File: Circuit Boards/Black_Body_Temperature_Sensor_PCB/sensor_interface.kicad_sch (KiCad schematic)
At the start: 5 parts, among them J1 Conn_01x04_Pin, Q8 TMUX1112PWR, Q9 TMUX1112PWR

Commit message: power simulation
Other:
- moved on the sheet: J1, Q8, Q9, R16, R17

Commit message: Schematic ready for review
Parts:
- added Q10: TMUX1112PWR, Package_SO:TSSOP-16_4.4x5mm_P0.65mm, symbol -fet:TMUX1112PWR
- added R36: 5, symbol Device:R
- added R37: 500, symbol Device:R
- added R38: 35k, symbol Device:R
- R16, R17: now not fitted
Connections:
- net +3V3: now also Q10.13 (VDD)
- net GNDPWR: now also Q10.5 (GND)
- net i+: now also Q10.2 (D1), R36.1, R37.1, R38.1; no longer Q8.15 (D2), Q8.2 (D1)
- new net: Q10.15 (D2), R36.2
- new net: Q10.7 (D4), R38.2
- new net: Q10.10 (D3), R37.2
- new net: Q10.12 (NC), Q10.4 (NC)
- new net i_sense.I+: Q10.11 (S3), Q10.14 (S2), Q10.3 (S1), Q10.6 (S4), Q8.15 (D2), Q8.2 (D1)
- new net i_sense_sel1: Q10.1 (SEL1)
- new net i_sense_sel2: Q10.16 (SEL2)
- new net i_sense_sel3: Q10.9 (SEL3)
- new net i_sense_sel4: Q10.8 (SEL4)
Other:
- moved on the sheet: Q8, Q9

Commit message: Temp sensor schematic done
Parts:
- removed J1: Conn_01x04_Pin, symbol Connector:Conn_01x04_Pin
- added J401, J402: Screw_Terminal_01x02, TerminalBlock_MetzConnect:TerminalBlock_MetzConnect_Type011_RT05502HBLC_1x02_P5.00mm_Horizontal, symbol Connector:Screw_Terminal_01x02
- R401: renamed from R36; footprint (none) -> Resistor_SMD:R_0603_1608Metric
- R402: renamed from R37; footprint (none) -> Resistor_SMD:R_0603_1608Metric
- R403: renamed from R38; footprint (none) -> Resistor_SMD:R_0603_1608Metric
- R404: renamed from R16; footprint (none) -> Resistor_SMD:R_0603_1608Metric
- R405: renamed from R17; footprint (none) -> Resistor_SMD:R_0603_1608Metric
- renumbered Q10 to Q401, Q8 to Q402, Q9 to Q403
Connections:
- net i+: now also J402.1 (Pin_1)
- net i-: now also J402.2 (Pin_2)
- net v_sense.V+: now also J401.1 (Pin_1)
- net v_sense.V-: now also J401.2 (Pin_2)
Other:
- note added: "Sensor Interface (PAGE 4)"
- moved on the sheet: Q401, Q402, Q403, R401, R402, R403, R404, R405

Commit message: temp pcb analog layout done
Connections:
- net GND: now also Q402.3 (S1); no longer Q402.14 (S2)
- net i-: now also Q402.15 (D2), Q402.2 (D1); no longer Q402.10 (D3), Q402.7 (D4)
- net i_sense.I+: now also Q402.10 (D3), Q402.7 (D4); no longer Q402.15 (D2), Q402.2 (D1)
- net at R404.1: now also Q403.3 (S1); no longer Q403.14 (S2)
- net I_Source: now reaches Q402.11 (S3), Q403.11 (S3)
- net I_Source: now also Q402.14 (S2), Q403.14 (S2)

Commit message: Digital section done
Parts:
- J401, J402: footprint TerminalBlock_MetzConnect:TerminalBlock_MetzConnect_Type011_RT05502HBLC_1x02_P5.00mm_Horizontal -> -connector:CUI_TB002-500-02BE
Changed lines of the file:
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@@
 			)
 		)
-		(property "Footprint" "TerminalBlock_MetzConnect:TerminalBlock_MetzConnect_Type011_RT05502HBLC_1x02_P5.00mm_Horizontal"
+		(property "Footprint" "-connector:CUI_TB002-500-02BE"
 			(at 50.8 101.6 0)
 			(hide yes)
@@
 	)
 	(symbol
+		(lib_id "Connector:Screw_Terminal_01x02")
+		(at 50.8 106.68 0)
+		(mirror y)
+		(unit 1)
+		(body_style 1)
+		(exclude_from_sim no)
+		(in_bom yes)
+		(on_board yes)
+		(in_pos_files yes)
+		(dnp no)
+		(property "Reference" "J402"
+			(at 48.26 106.6799 0)
+			(show_name no)
+			(do_not_autoplace no)
+			(effects
+				(font
+					(size 1.27 1.27)
+				)
+				(justify left)
+			)
+		)
+		(property "Value" "Screw_Terminal_01x02"
+			(at 48.26 109.2199 0)
+			(show_name no)
+			(do_not_autoplace no)
+			(effects
+				(font
+					(size 1.27 1.27)
+				)
+				(justify left)
+			)
+		)
+		(property "Footprint" "-connector:CUI_TB002-500-02BE"
+			(at 50.8 106.68 0)
+			(hide yes)
+			(show_name no)
+			(do_not_autoplace no)
+			(effects
+				(font
+					(size 1.27 1.27)
+				)
+			)
+		)
+		(property "Datasheet" ""
+			(at 50.8 106.68 0)
+			(hide yes)
+			(show_name no)
+			(do_not_autoplace no)
+			(effects
+				(font
+					(size 1.27 1.27)
+				)
+			)
+		)
+		(property "Description" "Generic screw terminal, single row, 01x02, script generated (kicad-library-utils/schlib/autogen/connector/)"
+			(at 50.8 106.68 0)
+			(hide yes)
+			(show_name no)
+			(do_not_autoplace no)
+			(effects
+				(font
+					(size 1.27 1.27)
+				)
+			)
+		)
+		(pin "1"
+		)
+		(pin "2"
+		)
+		(instances
+			(project "Black_Body_Temperature_Sensor_PCB"
+				(path "/e46fba8d-0294-4f4f-927d-8614bb9d51d3/4094c958-ded6-41d9-bb08-a88dca4a947b"
+					(reference "J402")
+					(unit 1)
+				)
+			)
+		)
+	)
+	(symbol
 		(lib_id "Device:R")
 		(at 104.14 82.55 90)
@@
 					(unit 1)
 				)
-			)
-		)
-	)
-	(symbol
-		(lib_id "Connector:Screw_Terminal_01x02")
-		(at 50.8 106.68 0)
-		(mirror y)
-		(unit 1)
-		(body_style 1)
-		(exclude_from_sim no)
-		(in_bom yes)
-		(on_board yes)
-		(in_pos_files yes)
-		(dnp no)
-		(property "Reference" "J402"
-			(at 48.26 106.6799 0)
-			(show_name no)
-			(do_not_autoplace no)
-			(effects
-				(font
-					(size 1.27 1.27)
-				)
-				(justify left)
-			)
-		)
-		(property "Value" "Screw_Terminal_01x02"
-			(at 48.26 109.2199 0)
-			(show_name no)
-			(do_not_autoplace no)
-			(effects
-				(font
-					(size 1.27 1.27)
-				)
-				(justify left)
-			)
-		)
-		(property "Footprint" "TerminalBlock_MetzConnect:TerminalBlock_MetzConnect_Type011_RT05502HBLC_1x02_P5.00mm_Horizontal"
-			(at 50.8 106.68 0)
-			(hide yes)
-			(show_name no)
-			(do_not_autoplace no)
-			(effects
-				(font
-					(size 1.27 1.27)
-				)
-			)
-		)
-		(property "Datasheet" ""
-			(at 50.8 106.68 0)
-			(hide yes)
-			(show_name no)
-			(do_not_autoplace no)
-			(effects
-				(font
-					(size 1.27 1.27)
-				)
-			)
-		)
-		(property "Description" "Generic screw terminal, single row, 01x02, script generated (kicad-library-utils/schlib/autogen/connector/)"
-			(at 50.8 106.68 0)
-			(hide yes)
-			(show_name no)
-			(do_not_autoplace no)
-			(effects
-				(font
-					(size 1.27 1.27)
-				)
-			)
-		)
-		(pin "1"
-		)
-		(pin "2"
-		)
-		(instances
-			(project "Black_Body_Temperature_Sensor_PCB"
-				(path "/e46fba8d-0294-4f4f-927d-8614bb9d51d3/4094c958-ded6-41d9-bb08-a88dca4a947b"
-					(reference "J402")
-					(unit 1)
-				)

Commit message: Complete except for recommended changes
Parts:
- added C401, C402, C403, C404, C405, C406, C407, C408, C409, C410, C411, C412, C413, C414, C415, C416, C417, C418, C419, C420, C421, C422, C423, C424: 2u2, Capacitor_SMD:C_0402_1005Metric, symbol Device:C
- added R401, R402, R403, R404, R408, R409, R410, R411, R414, R415, R416, R417: 5.1k, Resistor_SMD:R_0402_1005Metric, symbol Device:R
- added TP401, TP402, TP403: TestPoint, TestPoint:TestPoint_Pad_2.0x2.0mm, symbol Connector:TestPoint
- renumbered R401 to R405, R402 to R406, R403 to R407, R404 to R412, R405 to R413
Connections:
- net GNDPWR: now also C401.2, C402.2, C403.2, C404.2, C405.2, C406.2, C407.2, C408.2, C409.2, C410.2, C411.2, C412.2, C413.2, C414.2, C415.2, C416.2, C417.2, C418.2, C419.2, C420.2, C421.2, C422.2, C423.2, C424.2
- net I_Source: now also TP401.1
- net hbridge_sel1: now also C413.1, R408.2; no longer Q402.1 (SEL1)
- net hbridge_sel2: now also C414.1, R409.2; no longer Q402.16 (SEL2)
- net hbridge_sel3: now also C415.1, R410.2; no longer Q402.9 (SEL3)
- net hbridge_sel4: now also C416.1, R411.2; no longer Q402.8 (SEL4)
- net i_sense_sel1: now also C405.1, R401.2; no longer Q401.1 (SEL1)
- net i_sense_sel2: now also C406.1, R402.2; no longer Q401.16 (SEL2)
- net i_sense_sel3: now also C407.1, R403.2; no longer Q401.9 (SEL3)
- net i_sense_sel4: now also C408.1, R404.2; no longer Q401.8 (SEL4)
- net i_source_sel1: now also C421.1, R414.2; no longer Q403.1 (SEL1)
- net i_source_sel2: now also C422.1, R415.2; no longer Q403.16 (SEL2)
- net i_source_sel3: now also C423.1, R416.2; no longer Q403.9 (SEL3)
- net i_source_sel4: now also C424.1, R417.2; no longer Q403.8 (SEL4)
- net nA_I_Source: now also TP403.1
- net uA_I_Source: now also TP402.1
- new net selh1: C409.1, Q402.1 (SEL1), R408.1
- new net selh2: C410.1, Q402.16 (SEL2), R409.1
- new net selh3: C411.1, Q402.9 (SEL3), R410.1
- new net selh4: C412.1, Q402.8 (SEL4), R411.1
- new net seli1: C401.1, Q401.1 (SEL1), R401.1
- new net seli2: C402.1, Q401.16 (SEL2), R402.1
- new net seli3: C403.1, Q401.9 (SEL3), R403.1
- new net seli4: C404.1, Q401.8 (SEL4), R404.1
- new net sels1: C417.1, Q403.1 (SEL1), R414.1
- new net sels2: C418.1, Q403.16 (SEL2), R415.1
- new net sels3: C419.1, Q403.9 (SEL3), R416.1
- new net sels4: C420.1, Q403.8 (SEL4), R417.1

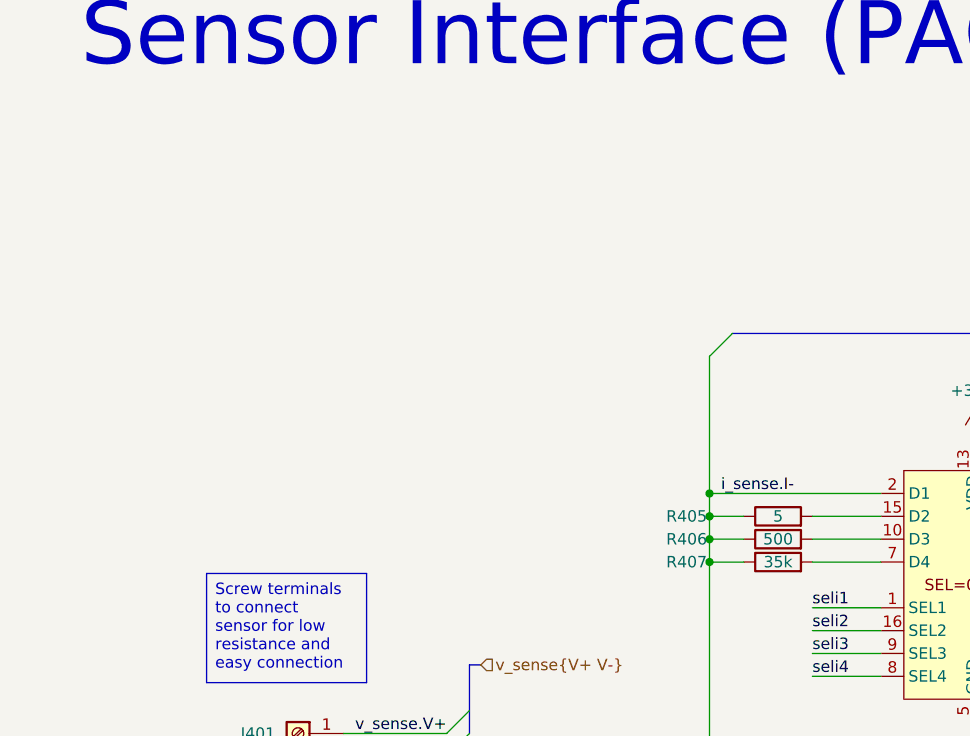
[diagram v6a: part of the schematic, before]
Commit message: Temp probe bom done
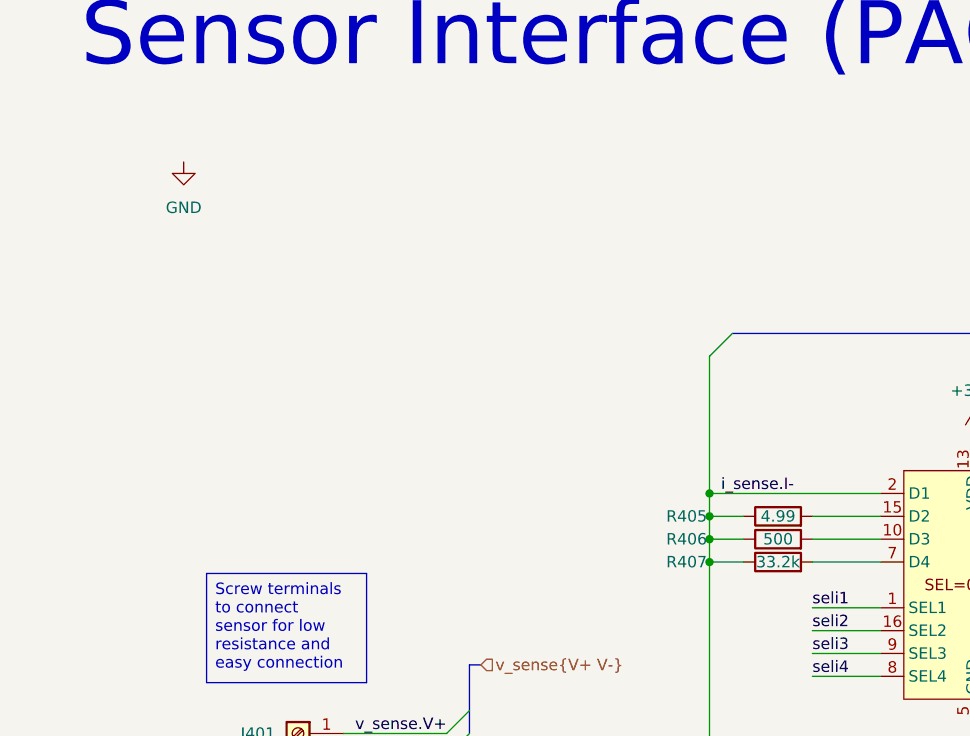
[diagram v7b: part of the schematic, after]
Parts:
- C401, C402, C403, C404, C405, C406, C407, C408, C409, C410, C411, C412, C413, C414, C415, C416, C417, C418, C419, C420, C421, C422, C423, C424: MPN (none) -> GRM155R61E225ME15D
- J401, J402: MPN (none) -> TB002-500-02BE
- Q401, Q402, Q403: MPN (none) -> TMUX1112PWR
- R401, R402, R403, R404, R408, R409, R410, R411, R414, R415, R416, R417: MPN (none) -> RT0402BRD075K1L
- R405: value 5 -> 4.99; MPN (none) -> RN73C1J4R99BTD
- R406: MPN (none) -> ERA-3AEB4990V
- R407: value 35k -> 33.2k; MPN (none) -> ERA-3AEB3322V
- R412, R413: MPN (none) -> ERA-3AEB103V
